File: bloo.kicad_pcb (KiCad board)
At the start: 2 copper layers, 84 parts, among them M1 M1_Conn_Alt, M2 M2_Conn_Alt, Q0 TEFT4300, Q1 TEFT4300, Q10 Q_NMOS_GSD, Q11 Q_NMOS_GSD, Q12 Q_NMOS_GSD, Q2 TEFT4300, Q3 TEFT4300, Q9 Q_NMOS_GSD, SW1 SW, SW2 SW, SW3 SW, U1 YAAJ_BluePill_SWD_Breakout, U2 L293D, U3 LM1085-5.0, U4 APE8865Y5-33-HF-3

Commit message: started layout
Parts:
- added C5: 100nF, Capacitor_SMD:C_0603_1608Metric, F.Cu at (288.7, 127.0)
- added C6: 47µF, Capacitor_SMD:C_1206_3216Metric, F.Cu at (285.3, 127.1)
- added J5: SWD_Header, Connector_PinHeader_2.54mm:PinHeader_1x05_P2.54mm_Vertical, F.Cu at (276.3, 115.6)
- added R10: 10k, Resistor_SMD:R_1206_3216Metric_Pad1.30x1.75mm_HandSolder, F.Cu at (285.3, 121.4)
- added U5: BC832, custom_foot:XCVR_BC832, F.Cu at (278.4, 124.4)
- M1, M2: footprint Connector_PinHeader_2.54mm:PinHeader_1x06_P2.54mm_Vertical -> MM_Library:Motor Headers
- moved M_MH2 192.9 mm to (256.7, 104.3), turned to 180 degrees
- moved U3 191.1 mm to (229.4, 111.1), turned to 180 degrees
- moved M_MH1 181.9 mm to (242.3, 104.3)
- moved S1 181.8 mm to (237.8, 119.1), turned to -90 degrees
- moved M1 173.2 mm to (268.9, 85.1), turned to 180 degrees
- moved U2 171.6 mm to (258.1, 87.5), turned to -90 degrees
- moved U1 171.3 mm to (247.5, 74.3), turned to 90 degrees
- moved BT1 150.0 mm to (235.4, 127.7), turned to -90 degrees
- moved M2 137.6 mm to (228.7, 85.2), turned to 180 degrees
- moved U4 30.0 mm to (56.6, 148.9)
- moved JP4 29.4 mm to (86.2, 172.1)
- moved TP6 27.8 mm to (94.2, 160.4)
- moved TP5 21.6 mm to (54.6, 136.2)
- moved TP2 6.15 mm to (60.8, 139.7)
- moved D6 4.93 mm to (85.8, 139.8)
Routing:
- added copper zone on F.Cu, net GND
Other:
- board outline added: 85 x 85 mm

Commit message: edgecut edits + adding on layout
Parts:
- moved Q3 234.4 mm to (215.5, 317.4), turned to 180 degrees
- moved C4 227.4 mm to (260.9, 89.4), turned to 90 degrees
- moved R4 225.7 mm to (198.9, 268.2)
- moved C14 225.7 mm to (148.8, 317.2)
- moved C15 225.7 mm to (148.8, 320.6)
- moved C20 225.7 mm to (154.8, 313.9)
- moved C21 225.7 mm to (154.8, 317.2)
- moved Q0 225.7 mm to (195.9, 309.1)
- moved Q1 225.7 mm to (201.5, 309.1)
- moved Q2 225.7 mm to (207.1, 309.1)
- moved R1 225.7 mm to (198.9, 258.3)
- moved R2 225.7 mm to (198.9, 261.6)
- moved R3 225.7 mm to (198.9, 264.9)
- moved C10 212.5 mm to (247.8, 129.0), turned to -90 degrees
- moved C13 209.7 mm to (250.6, 129.0), turned to -90 degrees
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- renumbered TP3 to 5V_TP, TP6 to GND, JP4 to JP
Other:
- board size 85 x 85 mm -> 80 x 92.4 mm

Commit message: placed shi
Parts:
- 5V: renamed from 5V_TP; value TP_5V -> 5V
- moved D4 203.9 mm to (223.7, 81.2), turned to 90 degrees
- moved R19 203.0 mm to (224.1, 75.8), turned to 90 degrees
- moved D5 199.0 mm to (219.2, 81.2), turned to 90 degrees
- moved R21 198.9 mm to (221.6, 75.8), turned to 90 degrees
- moved R20 197.3 mm to (219.1, 75.8), turned to 90 degrees
- moved D6 195.8 mm to (221.5, 81.2), turned to 90 degrees
- moved R8 122.4 mm to (42.4, 232.4)
- moved R23 112.9 mm to (256.7, 59.7), turned to 90 degrees
- moved R13 110.6 mm to (48.2, 232.1)
- moved R14 110.6 mm to (48.2, 235.4)
- moved R15 110.6 mm to (48.2, 238.7)
- moved R16 110.6 mm to (48.2, 242.0)
- moved R5 110.6 mm to (42.2, 235.4)
- moved R6 110.6 mm to (42.2, 238.7)
- moved R7 110.6 mm to (42.2, 242.0)
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- renumbered TP4 to 3V, TP5 to GND
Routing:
- net +3V3: track 0.00 -> 6.81 mm
- net BT_RESET: track 0.00 -> 3.06 mm
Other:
- board size 80 x 92.4 mm -> 90 x 96 mm
- board text added: "Buttons"
- board text added: "Emitters"
- board text added: "Receivers"

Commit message: continued layout for IR and buttons
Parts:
- moved Q9 311.4 mm to (273.7, 59.5)
- moved D0 310.7 mm to (291.6, 64.2), turned to 180 degrees
- moved Q10 296.5 mm to (246.4, 55.3), turned to 90 degrees
- moved D1 295.1 mm to (263.2, 48.4), turned to 120 degrees
- moved R5 293.9 mm to (278.5, 60.6), turned to 180 degrees
- moved Q11 292.9 mm to (235.8, 54.2), turned to 90 degrees
- moved Q12 288.5 mm to (230.9, 60.2), turned to 180 degrees
- moved D2 281.5 mm to (247.3, 46.1), turned to -120 degrees
- moved R13 281.3 mm to (270.3, 59.4), turned to 90 degrees
- moved R6 278.3 mm to (251.9, 55.7), turned to 180 degrees
- moved R7 269.3 mm to (240.1, 59.4), turned to -90 degrees
- moved R14 265.1 mm to (246.0, 59.0), turned to 180 degrees
- moved R16 261.1 mm to (236.0, 60.7), turned to 180 degrees
- moved R15 260.6 mm to (236.0, 58.0), turned to 180 degrees
- moved R8 246.8 mm to (224.0, 65.3)
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
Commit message: started routing
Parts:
- removed 3V: TP_3V3, Connector_PinHeader_2.54mm:PinHeader_1x01_P2.54mm_Vertical
- removed the GND at (256.4, 125.2)
- removed the GND at (294.8, 64.4)
- removed JP: Jumper_2_Open, Jumper:SolderJumper-2_P1.3mm_Bridged_Pad1.0x1.5mm
- added 3V3: TP_3V3, Connector_PinHeader_2.54mm:PinHeader_1x01_P2.54mm_Vertical, F.Cu at (214.9, 82.5)
- added GND: GND_TP, Connector_PinHeader_2.54mm:PinHeader_1x01_P2.54mm_Vertical, F.Cu at (256.2, 127.3)
- added GND: GND_TP, Connector_PinHeader_2.54mm:PinHeader_1x01_P2.54mm_Vertical, F.Cu at (284.6, 65.2)
- added JP4: Jumper_2_Open, Jumper:SolderJumper-2_P1.3mm_Bridged_Pad1.0x1.5mm, F.Cu at (226.0, 117.3)
- 5V: value 5V -> TP_5V
- moved D5 25.6 mm to (242.4, 92.2), turned to 180 degrees
- moved R20 24.8 mm to (237.4, 92.5), turned to 180 degrees
- moved D6 22.7 mm to (242.4, 89.9), turned to 180 degrees
- moved R21 21.3 mm to (237.5, 90.0), turned to 180 degrees
- moved D4 19.9 mm to (242.4, 87.8), turned to 180 degrees
- moved R19 17.8 mm to (237.4, 87.5), turned to 180 degrees
- moved C25 10.7 mm to (215.0, 77.4)
- moved C18 10.6 mm to (220.7, 77.8), turned to 0 degrees
- moved C17 9.47 mm to (214.9, 69.8), turned to 180 degrees
- moved L1 9.39 mm to (220.7, 69.7), turned to 0 degrees
- moved C3 7.60 mm to (256.2, 122.4), turned to 180 degrees
- moved C11 6.72 mm to (220.7, 75.1), turned to 0 degrees
- moved C12 6.22 mm to (220.7, 72.4), turned to 0 degrees
- moved U4 5.20 mm to (215.7, 73.7), turned to -90 degrees
- moved R8 2.55 mm to (224.0, 62.8)
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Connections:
- 5V pad 1: +5V_NET -> +5V
- C1 pad 2: BATT_NET -> VCC
- C10 pad 1: +5V_NET -> +5V
- C13 pad 1: +5V_NET -> +5V
- C16 pad 1: +5V_NET -> +5V
- C2 pad 1: BATT_NET -> VCC
- C9 pad 1: BATT_NET -> VCC
- S1 pad 2: BATT_NET -> VCC
- U1 pad 11: SWO -> unconnected-(U1-PB3-Pad11)
- U3 pad 2: +5V_NET -> +5V
- U3 pad 3: BATT_NET -> VCC
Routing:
- net +3V3: track 6.81 -> 213.7 mm, vias 0 -> 1
- net +5V: track 0.00 -> 138.3 mm
- net USART1_TX: track 0.00 -> 101.9 mm, vias 0 -> 2
- net M2_SPD: track 0.00 -> 99.1 mm, vias 0 -> 1
- net USART1_RX: track 0.00 -> 98.0 mm, vias 0 -> 2
- net BLE_STATE: track 0.00 -> 92.6 mm, vias 0 -> 1
- net +3.3VA: track 0.00 -> 86.4 mm
- net M1_FWD: track 0.00 -> 78.9 mm
- net M1_SPD: track 0.00 -> 72.2 mm
- net VCC: track 0.00 -> 58.1 mm
- net RECEIV_3: track 0.00 -> 48.5 mm
- net RECEIV_4: track 0.00 -> 38.5 mm
- net M1_OUT_1: track 0.00 -> 38.1 mm
- net M1_OUT_2: track 0.00 -> 31.0 mm
- net BT_SWDIO: track 0.00 -> 25.2 mm
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
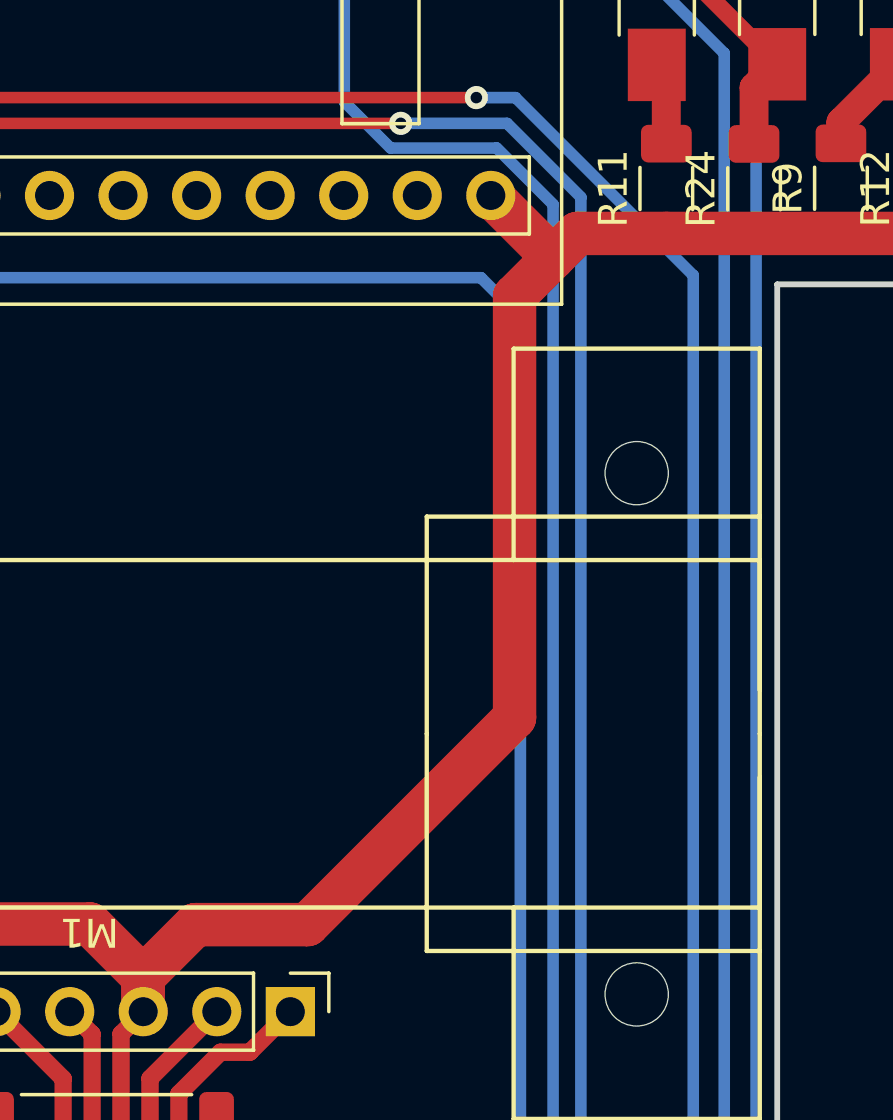
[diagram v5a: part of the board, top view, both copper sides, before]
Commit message: additional routing change
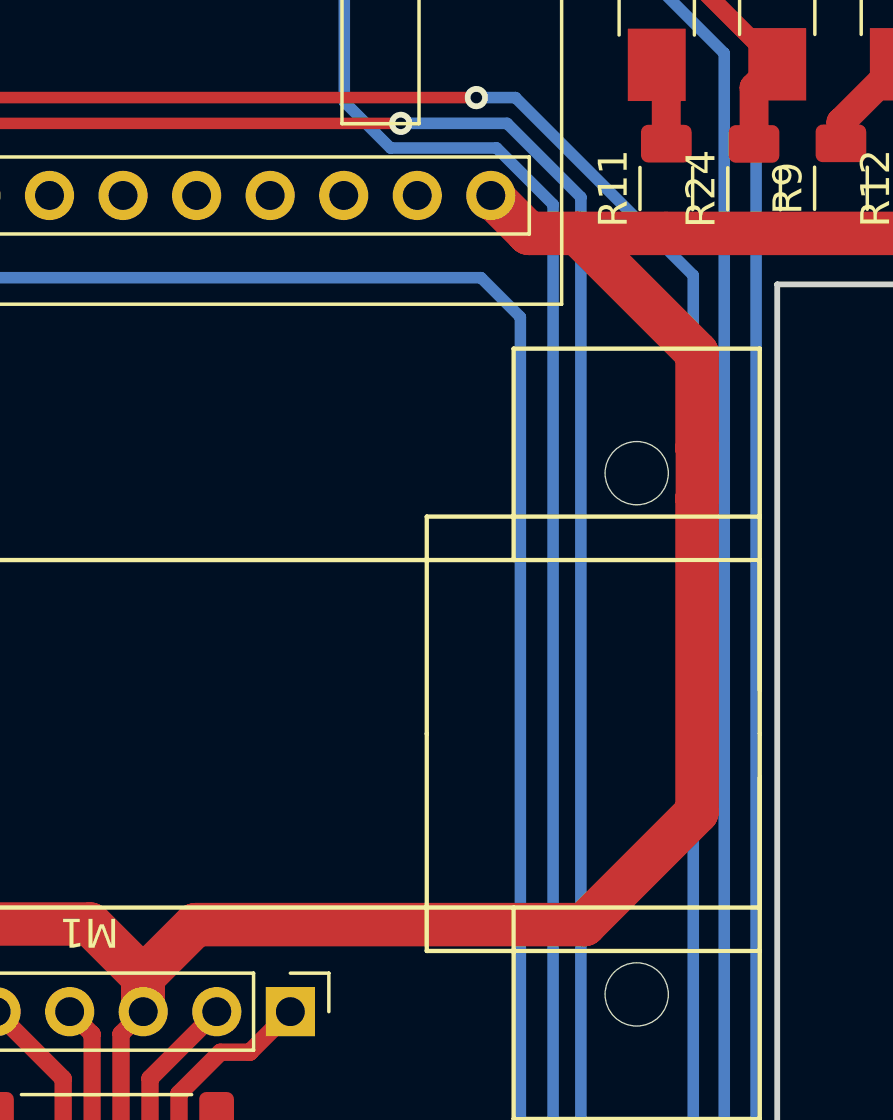
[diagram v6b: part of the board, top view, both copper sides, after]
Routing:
- net +3V3: track 213.7 -> 223.3 mm
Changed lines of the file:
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@@
+	)
+	(segment
+		(start 284.73 92.497732)
+		(end 284.7407 92.487032)
+		(width 1.5)
+		(layer "F.Cu")
+		(net 5)
+	)
+	(segment
+		(start 267.410319 107.21)
+		(end 280.84 107.21)
+		(width 1.5)
+		(layer "F.Cu")
+		(net 5)
 	)
 	(segment
@@
 	)
 	(segment
+		(start 284.73 90.742268)
+		(end 284.73 87.47)
+		(width 1.5)
+		(layer "F.Cu")
+		(net 5)
+	)
+	(segment
 		(start 235.9 87.48)
 		(end 225.75 87.48)
@@
 	)
 	(segment
+		(start 247.977719 107.19)
+		(end 263.77 107.19)
+		(width 1.5)
+		(layer "F.Cu")
+		(net 5)
+	)
+	(segment
+		(start 235.9 92.47)
+		(end 235.9 87.48)
+		(width 1.5)
+		(layer "F.Cu")
+		(net 5)
+	)
+	(segment
+		(start 225.75 87.48)
+		(end 220.71 82.44)
+		(width 1.5)
+		(layer "F.Cu")
+		(net 5)
+	)
+	(segment
+		(start 246.0432 109.124519)
+		(end 243.988681 107.07)
+		(width 1.5)
+		(layer "F.Cu")
+		(net 5)
+	)
+	(segment
+		(start 280.84 107.21)
+		(end 284.73 103.32)
+		(width 1.5)
+		(layer "F.Cu")
+		(net 5)
+	)
+	(segment
+		(start 219.18 69.715)
+		(end 219.18 77.765)
+		(width 1)
+		(layer "F.Cu")
+		(net 5)
+	)
+	(segment
+		(start 263.77 107.19)
+		(end 265.6066 109.0266)
+		(width 1.5)
+		(layer "F.Cu")
+		(net 5)
+	)
+	(segment
+		(start 284.7407 90.752968)
+		(end 284.73 90.742268)
+		(width 1.5)
+		(layer "F.Cu")
+		(net 5)
+	)
+	(segment
+		(start 246.0432 109.124519)
+		(end 247.977719 107.19)
+		(width 1.5)
+		(layer "F.Cu")
+		(net 5)
+	)
+	(segment
+		(start 284.73 87.47)
+		(end 280.6 83.34)
+		(width 1.5)
+		(layer "F.Cu")
+		(net 5)
+	)
+	(segment
+		(start 222.595 66.705)
+		(end 222.62 66.68)
+		(width 1)
+		(layer "F.Cu")
+		(net 5)
+	)
+	(segment
+		(start 246.0432 110.3266)
+		(end 245.2766 111.0932)
+		(width 0.6)
+		(layer "F.Cu")
+		(net 5)
+	)
+	(segment
+		(start 285.4825 133.609)
+		(end 285.4725 133.599)
+		(width 0.6)
+		(layer "F.Cu")
+		(net 5)
+	)
+	(segment
+		(start 284.73 103.32)
+		(end 284.73 92.497732)
+		(width 1.5)
+		(layer "F.Cu")
+		(net 5)
+	)
+	(segment
+		(start 219.135 77.81)
+		(end 219.135 78.225)
+		(width 1)
+		(layer "F.Cu")
+		(net 5)
+	)
+	(segment
+		(start 283.67 83.34)
+		(end 292.72 83.34)
+		(width 1.5)
+		(layer "F.Cu")
+		(net 5)
+	)
+	(segment
+		(start 287.6575 133.609)
+		(end 285.4825 133.609)
+		(width 0.6)
+		(layer "F.Cu")
+		(net 5)
+	)
+	(segment
+		(start 280.6 83.34)
+		(end 283.67 83.34)
+		(width 1.5)
+		(layer "F.Cu")
+		(net 5)
+	)
+	(segment
+		(start 283.4635 122.819)
+		(end 282.6125 123.67)
+		(width 1.5)
+		(layer "F.Cu")
+		(net 5)
+	)
+	(segment
+		(start 243.988681 107.07)
+		(end 227.21 107.07)
+		(width 1.5)
+		(layer "F.Cu")
+		(net 5)
+	)
+	(segment
+		(start 278.92 83.34)
+		(end 277.61 82.03)
+		(width 1.5)
+		(layer "F.Cu")
+		(net 5)
+	)
+	(segment
 		(start 265.6066 109.013719)
 		(end 267.410319 107.21)
@@
 	)
 	(segment
-		(start 247.977719 107.19)
-		(end 263.77 107.19)
-		(width 1.5)
-		(layer "F.Cu")
-		(net 5)
-	)
-	(segment
-		(start 235.9 92.47)
-		(end 235.9 87.48)
-		(width 1.5)
-		(layer "F.Cu")
-		(net 5)
-	)
-	(segment
-		(start 225.75 87.48)
-		(end 220.71 82.44)
-		(width 1.5)
-		(layer "F.Cu")
-		(net 5)
-	)
-	(segment
-		(start 246.0432 109.124519)
-		(end 243.988681 107.07)
-		(width 1.5)
-		(layer "F.Cu")
-		(net 5)
-	)
-	(segment
-		(start 219.18 69.715)
-		(end 219.18 77.765)
-		(width 1)
-		(layer "F.Cu")
-		(net 5)
-	)
-	(segment
-		(start 263.77 107.19)
-		(end 265.6066 109.0266)
-		(width 1.5)
-		(layer "F.Cu")
-		(net 5)
-	)
-	(segment
-		(start 278.43 85.51)
-		(end 279.76 84.18)
-		(width 1.5)
-		(layer "F.Cu")
-		(net 5)
-	)
-	(segment
-		(start 246.0432 109.124519)
-		(end 247.977719 107.19)
-		(width 1.5)
-		(layer "F.Cu")
-		(net 5)
-	)
-	(segment
-		(start 222.595 66.705)
-		(end 222.62 66.68)
-		(width 1)
-		(layer "F.Cu")
-		(net 5)
-	)
-	(segment
-		(start 246.0432 110.3266)
-		(end 245.2766 111.0932)
-		(width 0.6)
-		(layer "F.Cu")
-		(net 5)
-	)
-	(segment
-		(start 285.4825 133.609)
-		(end 285.4725 133.599)
-		(width 0.6)
-		(layer "F.Cu")
-		(net 5)
-	)
-	(segment
-		(start 278.43 100.06)
-		(end 278.43 85.51)
-		(width 1.5)
-		(layer "F.Cu")
-		(net 5)
-	)
-	(segment
-		(start 219.135 77.81)
-		(end 219.135 78.225)
-		(width 1)
-		(layer "F.Cu")
-		(net 5)
-	)
-	(segment
-		(start 283.67 83.34)
-		(end 292.72 83.34)
-		(width 1.5)
-		(layer "F.Cu")
-		(net 5)
-	)
-	(segment
-		(start 287.6575 133.609)
-		(end 285.4825 133.609)
-		(width 0.6)
-		(layer "F.Cu")
-		(net 5)
-	)
-	(segment
-		(start 283.4635 122.819)
-		(end 282.6125 123.67)
-		(width 1.5)
-		(layer "F.Cu")
-		(net 5)
-	)
-	(segment
-		(start 267.410319 107.21)
-		(end 271.28 107.21)
-		(width 1.5)
-		(layer "F.Cu")
-		(net 5)
-	)
-	(segment
-		(start 271.28 107.21)
-		(end 278.43 100.06)
-		(width 1.5)
-		(layer "F.Cu")
-		(net 5)
-	)
-	(segment
-		(start 243.988681 107.07)
-		(end 227.21 107.07)
-		(width 1.5)
-		(layer "F.Cu")
-		(net 5)
-	)
-	(segment
 		(start 282.6125 123.67)
 		(end 282.6125 128.04)
@@
 	)
 	(segment
-		(start 280.6 83.34)
-		(end 283.67 83.34)
+		(start 284.7407 92.487032)
+		(end 284.7407 90.752968)
 		(width 1.5)
 		(layer "F.Cu")
@@
 	)
 	(segment
+		(start 280.6 83.34)
+		(end 278.92 83.34)
+		(width 1.5)
+		(layer "F.Cu")
+		(net 5)
+	)
+	(segment
 		(start 220.71 82.44)
 		(end 220.69 82.46)
@@
 	)
 	(segment
+		(start 220.69 82.46)
+		(end 214.9 82.46)
+		(width 1.5)
+		(layer "F.Cu")
+		(net 5)
+	)
+	(segment
 		(start 265.6066 110.2158)
 		(end 265.6066 109.013719)
@@
 	)
 	(segment
-		(start 220.69 82.46)
-		(end 214.9 82.46)
-		(width 1.5)
-		(layer "F.Cu")
-		(net 5)
-	)
-	(segment
 		(start 284.6975 122.819)
 		(end 283.4635 122.819)
@@
 	)
 	(segment
-		(start 279.76 84.18)
-		(end 280.6 83.34)
-		(width 1.5)
-		(layer "F.Cu")
-		(net 5)
-	)
-	(segment
 		(start 219.0875 69.8075)
 		(end 219.18 69.715)
@@
 		(width 1.5)
 		(layer "F.Cu")
-		(net 5)
-	)
-	(segment
-		(start 279.76 84.18)
-		(end 277.61 82.03)
-		(width 1.5)
-		(layer "F.Cu")

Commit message: Continued routing
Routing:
- net EMIT_1: track 0.00 -> 117.9 mm, vias 0 -> 1
- net AGND: track 0.00 -> 117.1 mm, vias 0 -> 8
- net VCC: track 58.1 -> 172.7 mm, vias 0 -> 3
- net +5V: track 138.3 -> 241.3 mm, vias 0 -> 2
- net M2_BACK: track 0.00 -> 100.0 mm, vias 0 -> 1
- net BUTTON_3: track 3.56 -> 101.3 mm, vias 0 -> 5
- net M1_ENC_A: track 6.52 -> 83.7 mm, vias 0 -> 1
- net EMIT_4: track 0.00 -> 72.8 mm, vias 0 -> 5
- net BUTTON: track 2.86 -> 73.9 mm, vias 0 -> 3
- net M1_ENC_B: track 7.16 -> 77.6 mm, vias 0 -> 3
- net M2_FWD: track 0.00 -> 69.7 mm
- net RST: track 5.63 -> 70.0 mm, vias 0 -> 1
- net M1_BACK: track 0.00 -> 64.2 mm
- net M2_ENC_B: track 7.16 -> 62.6 mm, vias 0 -> 1
- net RECEIV_1: track 12.6 -> 68.0 mm, vias 1 -> 5
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- added copper zone on B.Cu, net GND
